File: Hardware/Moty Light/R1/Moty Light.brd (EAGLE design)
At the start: 46.4 x 45.7 mm, 20 parts, among them T1 2SC1815

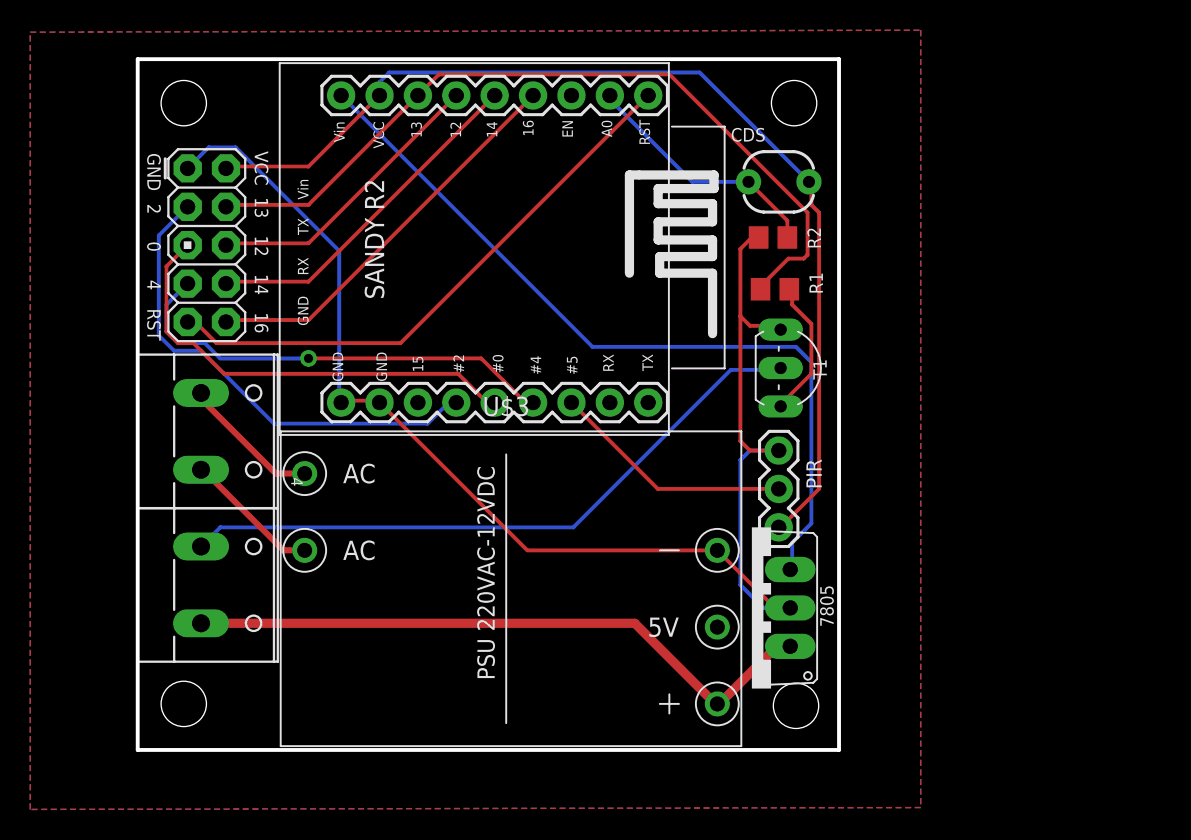
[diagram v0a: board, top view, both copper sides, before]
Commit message: Update design for Moty Light
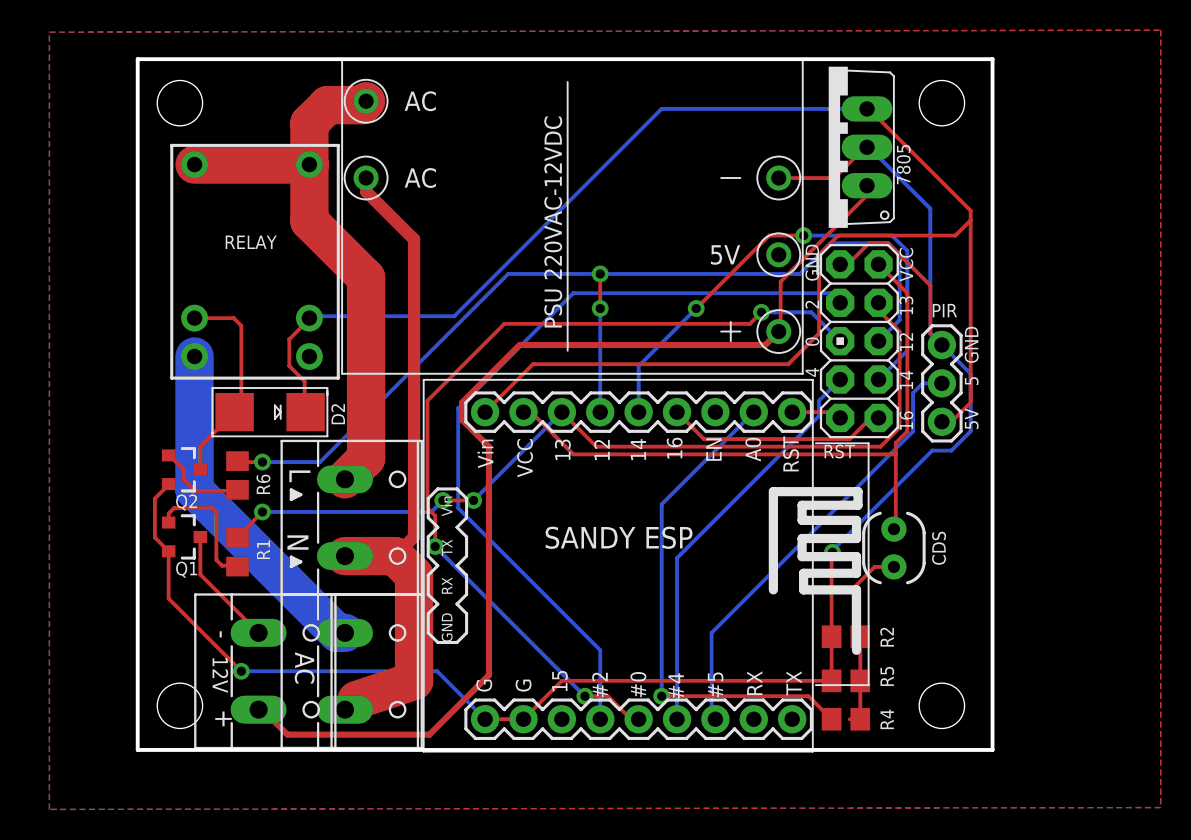
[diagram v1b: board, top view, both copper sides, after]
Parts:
- removed AC1: (no value), con-wago-508:W237-132
- removed T1: 2SC1815, transistor:TO92-ECB
- removed U$13, U$14: (no value), dicons:ICON_PIN1_B
- added 12V, AC_OUT: (no value), con-wago-508:W237-132
- added D2: (no value), adafruit:SMADIODE
- added Q1, Q2: C1815, SparkFun-DiscreteSemi:SOT23-3
- added R4: 220K, rcl:R0805
- added R5: 100K, rcl:R0805
- added R6: 1K, rcl:R0805
- added U$1: RELAY, My Eagle Lib:MINIATURE_RELAY_JRC_21F
- added U$4, U$5: (no value), dicons:ICON_PIN1_B
- R3: device SparkFun-Sensors:PHOTOCELL -> SparkFun-Sensors:PHOTOCELL_THIN
- moved JP2 43.6 mm to (70.7, 60.6)
- moved R1 39.6 mm to (29.6, 46.6), turned to 270 degrees
- moved 7805 30.9 mm to (68.7, 73.4)
- moved R2 26.9 mm to (69.8, 41.0)
- moved U$17 26.2 mm to (49.5, 63.5)
- moved R3 25.3 mm to (73.0, 47.0), turned to 270 degrees
- moved U$3 25.0 mm to (51.4, 68.8)
- moved U$2 23.0 mm to (54.6, 45.7)
- moved PIR 12.9 mm to (76.2, 60.3)
- moved U$12 11.6 mm to (33.8, 46.0), flipped to the top, turned to 180 degrees
- moved AC 11.1 mm to (37.3, 48.9)
- moved U$11 11.0 mm to (33.7, 52.3)
- moved U$8 9.78 mm to (76.2, 76.3)
- moved U$7 9.65 mm to (76.2, 36.4)
- moved U$6 0.28 mm to (25.8, 36.4)
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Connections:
- new net ADC: R2.2, R3.2, R4.2, R5.1
- new net N$3: D2.A, Q2.3, U$1.COIL2
- new net N$4: Q2.1, R6.2
- new net N$8: AC_OUT.1, U$1.NO
- net 12: now also R6.1
- net 12V: now also 12V.2; no longer AC1.2
- net 5V: now also D2.C, PIR.3, U$1.COIL1
- net A0: now also R4.1; no longer R2.2, R3.2
- net AC_L: now also U$1.COM1, U$1.COM2
- net AC_N: now also AC_OUT.2
- net GND: now also Q1.2, Q2.2, R5.2; no longer T1.E
- net N$1: now also 12V.1, Q1.3; no longer AC1.1, T1.C
- net N$7: now also Q1.1; no longer T1.B
- net VCC: no longer PIR.3
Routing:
- net 5V: track 52.8 -> 115.1 mm
- net 12: track 19.3 -> 65.6 mm, vias 0 -> 3
- net N$1: track 43.3 -> 7.95 mm
- net AC_N: track 9.07 -> 44.0 mm
- net RST: track 37.8 -> 3.33 mm
- net 12V: track 42.5 -> 71.6 mm
- net 0: track 30.0 -> 58.6 mm, vias 0 -> 3
- net AC_L: track 9.29 -> 37.6 mm
- net VCC: track 69.1 -> 44.5 mm
- net GND: track 94.2 -> 118.0 mm, vias 0 -> 2
- net N$8: track 0.00 -> 22.7 mm
- net 2: track 32.0 -> 53.2 mm
- net A0: track 16.4 -> 33.2 mm, vias 0 -> 1
- net N$3: track 0.00 -> 14.0 mm
- net 5: track 16.1 -> 29.4 mm
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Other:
- board size 46.4 x 45.7 mm -> 56.6 x 45.7 mm
- board text added: "+"
- board text added: "-"
- board text added: "5"
- board text added: "5V"
- board text added: "AC"
